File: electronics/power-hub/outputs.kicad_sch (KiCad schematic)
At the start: 72 parts, among them J2 ROW A, J3 ROW B, J4 ROW C, J5 ROW D, U11 TPS26600PWPR, U12 TPS26600PWPR, U13 TPS26600PWPR, U14 TPS26600PWPR

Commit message: PCBA review: hub and node fixes before the order
On main's CH224A hub and the bay node v0.5.

Power hub:
- CPL: the side LEDs (C598310, C4555382) +0.825 mm, their polarity
  proven from JLC's own footprints (and C495809 at 270 deg in the table,
  for the IRF7842 the AP33772S hub had).
- Rows: SHDN pull-downs 10k, so rows stay off without firmware (100k
  gave 1 V at the pin's 10 uA); a B5819W at each row output for the
  cable's kick; the red FAULT LEDs fed from their ROW_EN, so a row that
  is simply off shows no fault.
- In2's VRACK band 8 mm wide; the console's USB pair hand-routed on
  F.Cu over In1 (U5's channels in the pair's order), EN's capacitor at
  the module's pin; reliefs on both pads of C2, C10, R3, C11-C14; notes
  corrected, the outputs sheet on A2.
- The PESD2CAN kept and documented (no stocked CAN TVS stays off at
  29.4 V and clamps under +40 V).

Bay node:
- SW3 placed on its pegs (-0.55 mm, Shouhan's land pattern); 2.2k I2C
  pull-ups; POS_IN 470k; AUX_VREF 1k; 100k on SVC; U9's input on a +5V
  island with three vias, C20 at its pins; C12 relieved; the camera note
  and the catalog's MPN text corrected.

Both re-routed: ERC 0, DRC 0 (the known C8 silkscreen warning), parity
0; CPL audit against JLC's footprints: every part agrees but SW3's pads
(0.13 mm, on purpose).  Bring-up measurements in assembly.md, the
resolution in pcba-review.md.

Co-Authored-By: Claude Opus 5.5 <noreply@anthropic.com>
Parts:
- added D41, D42, D43, D44: B5819W SL, Diode_SMD:D_SOD-123, symbol Device:D_Schottky
- R71, R72, R73, R74: value 100k -> 10k; LCSC C25803 -> C25804; MPN 0603WAF1003T5E -> 0603WAF1002T5E
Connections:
- net +3V3: no longer R51.1, R52.1, R53.1, R54.1
- net GND: now also D41.2 (A), D42.2 (A), D43.2 (A), D44.2 (A)
- net ROW_A: now also D41.1 (K)
- net ROW_B: now also D42.1 (K)
- net ROW_C: now also D43.1 (K)
- net ROW_D: now also D44.1 (K)
- net ROW_EN_A: now also R51.1
- net ROW_EN_B: now also R52.1
- net ROW_EN_C: now also R53.1
- net ROW_EN_D: now also R54.1
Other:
- moved on the sheet: C12, C13, C14, C22, C23, C24, C32, C33, C34, C62, C63, C64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

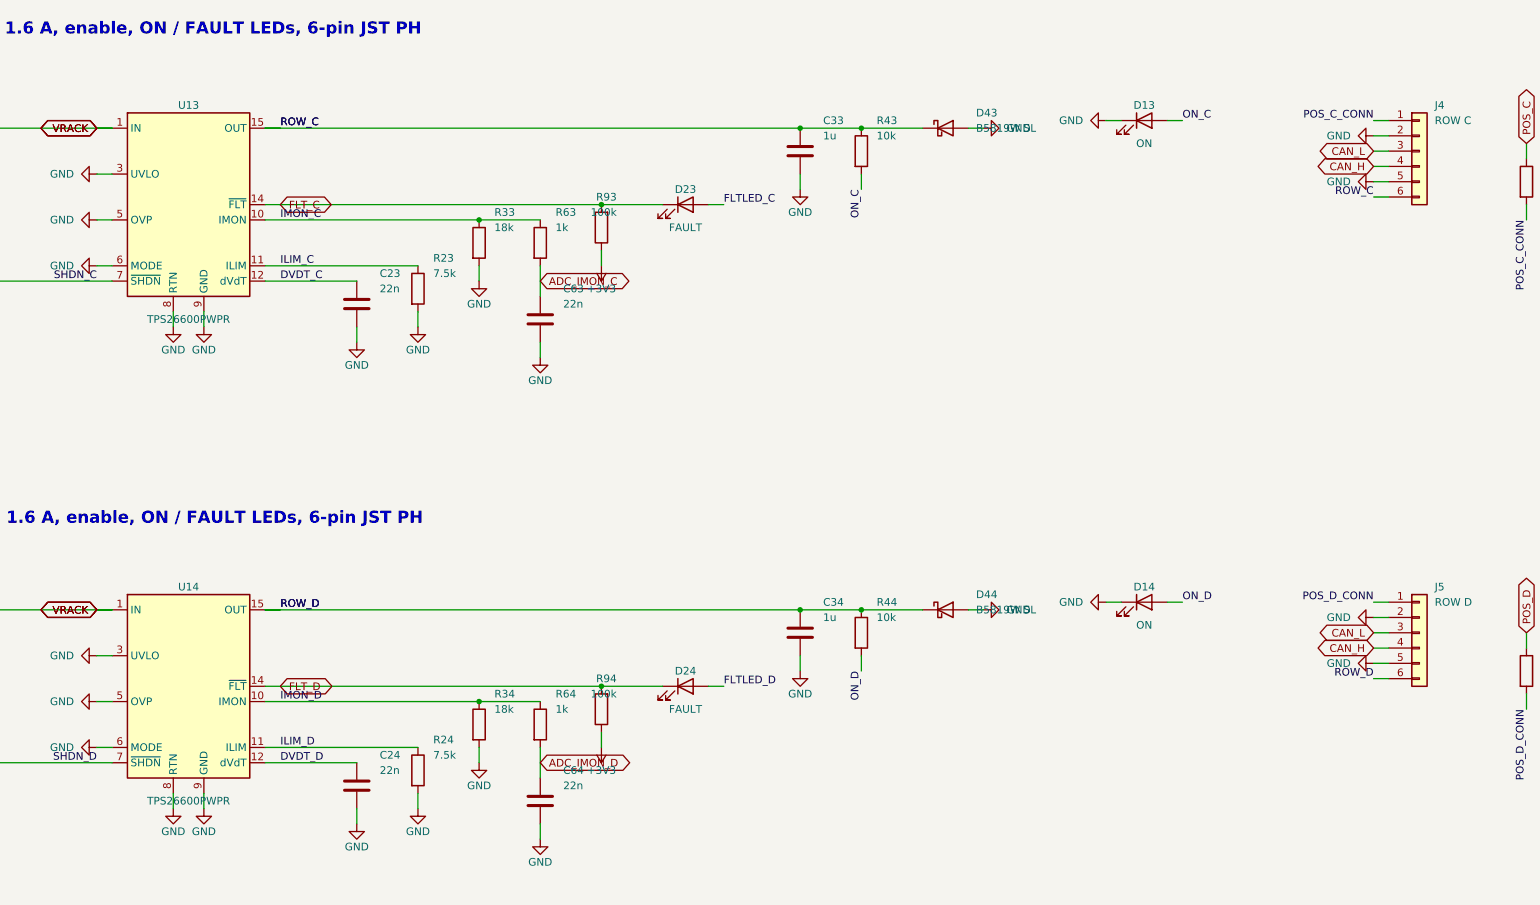
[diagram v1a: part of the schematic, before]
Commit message: Power hub: rows C and D not fitted for now
The user: "ne montons pas C et D pour l'instant".  The rack has two
rows, so the hub's rows C and D keep their footprints and routing, and
their costly parts are DNP:
- the eFuses U13/U14;
- the connectors J4/J5;
- the front LEDs D13/D14 (ON) and D23/D24 (FAULT).

Their passives stay: FLT's pull-up keeps FLT high and the IMON
resistor keeps IMON at 0 V, so the firmware sees no phantom fault or
current.  design.py's FITTED lists the fitted rows.

* The schematic and the PCB carry KiCad's DNP flag on those eight
  parts, set without touching placement or routing.  ERC 0, DRC 0,
  unconnected 0, parity 0.
* Fab outputs: the JLC BOM and CPL leave the eight out.  The Gerbers
  are unchanged (compared, member by member, minus dates).  The
  renders show the bare pads.
* The viewer shows the board as built: the fab GLB is exported with
  --no-dnp (the STEP keeps the DNP parts for fit checks).  The 3D
  coverage report lists them as "dnp", not missing.  The hub's viewer
  model is rebuilt.
* BOM regenerated.  The quote isn't repriced yet: the hub's balancing
  "components" line absorbs the difference until the cost session's
  pass.
* Docs: electronics.md and power.md say what refitting a row takes: a
  hot plate and hot air for the eFuse's pad, the LEDs on the box's
  holes, the devicetree, and the 140 W charger for a third row.

96 tools tests OK.

Co-Authored-By: Claude Opus 5.5 <noreply@anthropic.com>
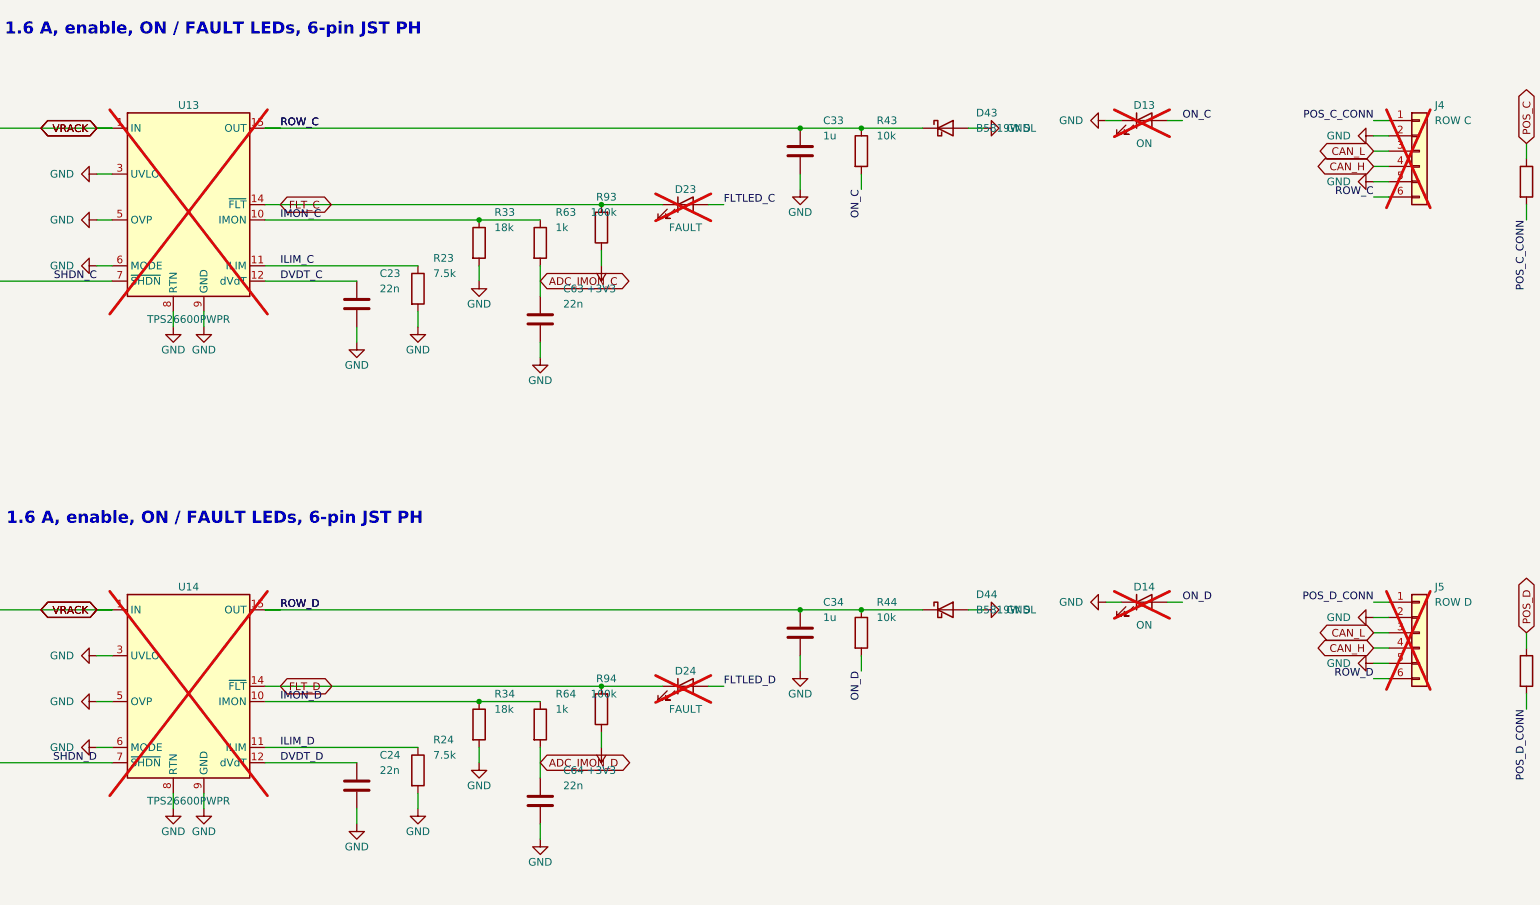
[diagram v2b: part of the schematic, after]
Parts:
- D13, D14, D23, D24, J4, J5, U13, U14: now not fitted
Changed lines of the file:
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@@
 		(in_bom yes)
 		(on_board yes)
-		(dnp no)
+		(dnp yes)
 		(fields_autoplaced yes)
 		(property "Reference" "U13"
@@
 		(in_bom yes)
 		(on_board yes)
-		(dnp no)
+		(dnp yes)
 		(fields_autoplaced yes)
 		(property "Reference" "D23"
@@
 		(in_bom yes)
 		(on_board yes)
-		(dnp no)
+		(dnp yes)
 		(fields_autoplaced yes)
 		(property "Reference" "D13"
@@
 		(in_bom yes)
 		(on_board yes)
-		(dnp no)
+		(dnp yes)
 		(fields_autoplaced yes)
 		(property "Reference" "J4"
@@
 		(in_bom yes)
 		(on_board yes)
-		(dnp no)
+		(dnp yes)
 		(fields_autoplaced yes)
 		(property "Reference" "U14"
@@
 		(in_bom yes)
 		(on_board yes)
-		(dnp no)
+		(dnp yes)
 		(fields_autoplaced yes)
 		(property "Reference" "D24"
@@
 		(in_bom yes)
 		(on_board yes)
-		(dnp no)
+		(dnp yes)
 		(fields_autoplaced yes)
 		(property "Reference" "D14"
@@
 		(in_bom yes)
 		(on_board yes)
-		(dnp no)
+		(dnp yes)
 		(fields_autoplaced yes)
 		(property "Reference" "J5"

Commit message: Power hub: 47 nF soft start, the LMR51625, the controller sheet on A2
Fixes from the schematic counter-review that the user approved.

* Every 22 nF goes to 47 nF.  The new part is C1622 (basic, the same
  0603 pads).  It covers C21-C24 (eFuse dVdT), C61-C64 (the IMON
  filter, now 47 us) and C118/C119 (the CAN split terminations).
  - A row of four nodes is about 450 uF.  With 22 nF the soft start
    charged it at about 2.6 A, over the 1.6 A limit.
  - With 47 nF it charges at about 1.2 A.  The ramp is 7.5 ms at 20 V
    and 10.5 ms at 28 V (t = 8e3 x V_IN x C_dVdT).
  - passives.py and its cache gain the 47 nF.
* The hub firmware's FLT blanking goes from 10 ms to 25 ms
  (HUB_ROW_FLT_BLANK_MS).  The TPS2660 asserts FLT through its soft
  start, and at 28 V that start now lasts 10.5 ms, longer than 10 ms.
* The buck changes from the LMR51635 to the LMR51625 with the 4.7 uH
  FXL0630-4R7-M.  These are the node's pair (buck25 / buck_l47, TI
  SLUSF64B table 8-1).
  - The controller takes under 0.7 A.
  - Same pinout and footprint, so the same 270 deg CPL correction.
* The routed PCB keeps its routing.  Only the properties of those 12
  footprints change (value, MPN, LCSC, description, datasheet).  They
  were copied from design.py with KiCad's Python, as pcbgen places
  them.
* The controller sheet (page 4) goes on A2, so the CAN block, the
  mounting holes and the notes are now on the page.
* Stale notes corrected:
  - the charger: 100 W at 20 V by default, 140 W EPR as an option;
  - the TPS26600's internal OVP is 31-34 V (typ 32.6 V), not 33 V
    (design.py, power.md, the devicetree comment);
  - the buck block now reads "from VRACK": there is no input switch
    any more.

Regenerated on zephyrbox with kicad.sh power-hub --check --fab.
- ERC 0, DRC 0, unconnected 0, parity 0.
- The Gerber zip and the top and iso renders are the same content.
  The bottom render's only difference was 9 pixels of raytracer
  noise in via holes, so it is kept.
- The viewer GLB com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
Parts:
- C21, C22, C23, C24, C61, C62, C63, C64: value 22n -> 47n; LCSC C21122 -> C1622; MPN CL10B223KB8NNNC -> CL10B473KB8NNNC
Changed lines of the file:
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@@
 			)
 		)
-		(property "Value" "22n"
+		(property "Value" "47n"
 			(at 120.65 71.12 0)
 			(effects
@@
 			)
 		)
-		(property "Description" "Capacitor 22n 0603"
+		(property "Description" "Capacitor 47n 0603"
 			(at 116.84 73.66 0)
 			(effects
@@
 			)
 		)
-		(property "LCSC" "C21122"
+		(property "LCSC" "C1622"
 			(at 116.84 73.66 0)
 			(effects
@@
 			)
 		)
-		(property "MPN" "CL10B223KB8NNNC"
+		(property "MPN" "CL10B473KB8NNNC"
 			(at 116.84 73.66 0)
 			(effects
@@
 			)
 		)
-		(property "Value" "22n"
+		(property "Value" "47n"
 			(at 151.13 73.66 0)
 			(effects
@@
 			)
 		)
-		(property "Description" "Capacitor 22n 0603"
+		(property "Description" "Capacitor 47n 0603"
 			(at 147.32 76.2 0)
 			(effects
@@
 			)
 		)
-		(property "LCSC" "C21122"
+		(property "LCSC" "C1622"
 			(at 147.32 76.2 0)
 			(effects
@@
 			)
 		)
-		(property "MPN" "CL10B223KB8NNNC"
+		(property "MPN" "CL10B473KB8NNNC"
 			(at 147.32 76.2 0)
 			(effects
@@
 			)
 		)
-		(property "Value" "22n"
+		(property "Value" "47n"
 			(at 120.65 151.13 0)
 			(effects
@@
 			)
 		)
-		(property "Description" "Capacitor 22n 0603"
+		(property "Description" "Capacitor 47n 0603"
 			(at 116.84 153.67 0)
 			(effects
@@
 			)
 		)
-		(property "LCSC" "C21122"
+		(property "LCSC" "C1622"
 			(at 116.84 153.67 0)
 			(effects
@@
 			)
 		)
-		(property "MPN" "CL10B223KB8NNNC"
+		(property "MPN" "CL10B473KB8NNNC"
 			(at 116.84 153.67 0)
 			(effects
@@
 			)
 		)
-		(property "Value" "22n"
+		(property "Value" "47n"
 			(at 151.13 153.67 0)
 			(effects
@@
 			)
 		)
-		(property "Description" "Capacitor 22n 0603"
+		(property "Description" "Capacitor 47n 0603"
 			(at 147.32 156.21 0)
 			(effects
@@
 			)
 		)
-		(property "LCSC" "C21122"
+		(property "LCSC" "C1622"
 			(at 147.32 156.21 0)
 			(effects
@@
 			)
 		)
-		(property "MPN" "CL10B223KB8NNNC"
+		(property "MPN" "CL10B473KB8NNNC"
 			(at 147.32 156.21 0)
 			(effects
@@
 			)
 		)
-		(property "Value" "22n"
+		(property "Value" "47n"
 			(at 120.65 232.41 0)
 			(effects
@@
 			)
 		)
-		(property "Description" "Capacitor 22n 0603"
+		(property "Description" "Capacitor 47n 0603"
 			(at 116.84 234.95 0)
 			(effects
@@
 			)
 		)
-		(property "LCSC" "C21122"
+		(property "LCSC" "C1622"
 			(at 116.84 234.95 0)
 			(effects
@@
 			)
 		)
-		(property "MPN" "CL10B223KB8NNNC"
+		(property "MPN" "CL10B473KB8NNNC"
 			(at 116.84 234.95 0)
 			(effects
@@
 			)
 		)
-		(property "Value" "22n"
+		(property "Value" "47n"
 			(at 151.13 234.95 0)
 			(effects
@@
 			)
 		)
-		(property "Description" "Capacitor 22n 0603"
+		(property "Description" "Capacitor 47n 0603"
 			(at 147.32 237.49 0)
 			(effects
@@
 			)
 		)
-		(property "LCSC" "C21122"
+		(property "LCSC" "C1622"
 			(at 147.32 237.49 0)
 			(effects
@@
 			)
 		)
-		(property "MPN" "CL10B223KB8NNNC"
+		(property "MPN" "CL10B473KB8NNNC"
 			(at 147.32 237.49 0)
 			(effects
@@
 			)
 		)
-		(property "Value" "22n"
+		(property "Value" "47n"
 			(at 120.65 312.42 0)
 			(effects
@@
 			)
 		)
-		(property "Description" "Capacitor 22n 0603"
+		(property "Description" "Capacitor 47n 0603"
 			(at 116.84 314.96 0)
 			(effects
@@
 			)
 		)
-		(property "LCSC" "C21122"
+		(property "LCSC" "C1622"
 			(at 116.84 314.96 0)
 			(effects
@@
 			)
 		)
-		(property "MPN" "CL10B223KB8NNNC"
+		(property "MPN" "CL10B473KB8NNNC"
 			(at 116.84 314.96 0)
 			(effects
@@
 			)
 		)
-		(property "Value" "22n"
+		(property "Value" "47n"
 			(at 151.13 314.96 0)
 			(effects
@@
 			)
 		)
-		(property "Description" "Capacitor 22n 0603"
+		(property "Description" "Capacitor 47n 0603"
 			(at 147.32 317.5 0)
 			(effects
@@
 			)
 		)
-		(property "LCSC" "C21122"
+		(property "LCSC" "C1622"
 			(at 147.32 317.5 0)
 			(effects
@@
 			)
 		)
-		(property "MPN" "CL10B223KB8NNNC"
+		(property "MPN" "CL10B473KB8NNNC"
 			(at 147.32 317.5 0)
 			(effects
@@
 		)
 	)
-	(text_box "TPS26600: I_LIM ≈ 12 A·kΩ / R_ILIM → 7.5k ≈ 1.6 A (JST PH: 2 A per contact).\nt_dVdT = 8e3 · V_IN · C_dVdT → 22 nF ≈ 3.5 ms at 20 V, 4.9 ms at 28 V.\nIMON: 78 µA/A into 18k → 1.4 V/A (2.2 V at the limit), 1k + 22 nF to the ESP32's ADC.\nSHDN: 10k to GND (row off: ≤ 10 µA from the pin, 0.1 V), ROW_EN through 10k → 1.65 V (on above 0.94 V).\nThe firmware holds ROW_EN with the ESP32's GPIO hold, so a controller reset leaves the rows as they were.\nFLT: open drain, 100k to 3.3 V for the controller; the red LED (1k) is fed from ROW_EN: it lights only for\n  a fault on an enabled row (FLT is also low while a row is off or starting).\nD41–D44 B5819W: GND → each row's output at its connector, for the cable's kick when the eFuse cuts a short.\nUVLO / OVP / MODE to GND: internal 15 V / 33 V thresholds, current-limit mode, auto-retry."
+	(text_box "TPS26600: I_LIM ≈ 12 A·kΩ / R_ILIM → 7.5k ≈ 1.6 A (JST PH: 2 A per contact).\nt_dVdT = 8e3 · V_IN · C_dVdT → 47 nF ≈ 7.5 ms at 20 V, 10.5 ms at 28 V.  A row of four nodes (≈ 450 µF)\n  then charges at C / (8e3 · C_dVdT) ≈ 1.2 A, under the 1.6 A limit (22 nF needed ≈ 2.6 A).\nIMON: 78 µA/A into 18k → 1.4 V/A (2.2 V at the limit), 1k + 47 nF (47 µs) to the ESP32's ADC.\nSHDN: 10k to GND (row off: ≤ 10 µA from the pin, 0.1 V), ROW_EN through 10k → 1.65 V (on above 0.94 V).\nThe firmware holds ROW_EN with the ESP32's GPIO hold, so a controller reset leaves the rows as they were.\nFLT: open drain, 100k to 3.3 V for the controller; the red LED (1k) is fed from ROW_EN: it lights only for\n  a fault on an enabled row (FLT is also low while a row is off or starting).\nD41–D44 B5819W: GND → each row's output at its connector, for the cable's kick when the eFuse cuts a short.\nUVLO / OVP / MODE to GND: internal 15 V / 31–34 V (typ 32.6 V) thresholds, current-limit mode, auto-retry."
 		(exclude_from_sim no)
 		(at 20.32 353.06 0)
-		(size 414.02 25.4)
+		(size 414.02 26.67)
 		(margins 1.5 1.5 1.5 1.5)
 		(stroke

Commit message: Schematic review S1, S4, S6: POS_IN 150k, the hub's ON LEDs on 18k, the camera's 0.75 A PTC
The user approved them ("S1 oui / S6 oui / S4 oui").

* S1, bay node: R29 470k -> 150k (C22807, basic).
  - Before its firmware runs, the upstream POS output (a node's IO42, the
    hub's IO10-13) floats. The BAT54S's warm leakage (about 2-3 uA at
    65 C) could then lift POS_IN through 470k to VIL.
  - Driven high through R30 + R28, 150k still gives 2.87 V, above VIH.
  - The design.py notes and bay_node.dtsi follow.
* S4, power hub: R41-R44 (the ON LEDs on the row outputs) 10k -> 18k
  (C25810, already on the board): 1.4 mA and 37 mW at 28 V. The 10k
  ran at 75 % of its 0603 rating at 29.4 V.
* S6, bay node: F1 (CAM_5V) goes from the 0.5 A PTC to SMD1206P075TF
  (RUILON, C20987, new catalog key pptc750): 0.75 A hold, 1.5 A trip,
  the same 1206 footprint. It is extended like C20799, so no fee changes.
  - Arducam gives the Mega 317 mA working: with the LEDs that is
    ~0.42 A on CAM_5V, where the 0.5 A part holds ~0.31 A at 70 C.
  - The camera pod's LDO tab gets the copper its routing leaves: a
    top-side +3V3 pour round the tab and a bottom-side island, joined by
    three vias. U1 drops ~0.5 W at 317 mA. The routing is unchanged.
  - The "~120 mA" notes go to 317 mA (node and pod design.py,
    electronics.md).
  - The bay's worst case follows: <= 2.25 A on +5V, the buck's inductor
    peaking at ~2.65 A (under its 2.9 A minimum limit), 13.5 W from
    VRACK (power-distribution-review.md, the buck notes).

The routed PCBs keep their routing.
- Node and hub: only the changed parts' properties (KiCad's Python, as
  pcbgen sets them).
- Pod: the two new zones and three vias, refilled.
- ERC 0, DRC 0, unconnected 0, parity 0 on all three (run on the Mac:
  zephyrbox didn't answer).
- keep_unchanged kept the node's renders and the hub's Gerbers. The
  hub's bottom render is restored: 9 pixels of via-hole noise, as before.
- The pod's renders, Gerbers and viewer GLB chang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
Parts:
- R41, R42, R43, R44: value 10k -> 18k; LCSC C25804 -> C25810; MPN 0603WAF1002T5E -> 0603WAF1802T5E
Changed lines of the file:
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@@
 			)
 		)
-		(property "Value" "10k"
+		(property "Value" "18k"
 			(at 203.2 45.72 0)
 			(effects
@@
 			)
 		)
-		(property "Description" "Resistor 10k 0603"
+		(property "Description" "Resistor 18k 0603"
 			(at 200.66 48.26 0)
 			(effects
@@
 			)
 		)
-		(property "LCSC" "C25804"
+		(property "LCSC" "C25810"
 			(at 200.66 48.26 0)
 			(effects
@@
 			)
 		)
-		(property "MPN" "0603WAF1002T5E"
+		(property "MPN" "0603WAF1802T5E"
 			(at 200.66 48.26 0)
 			(effects
@@
 			)
 		)
-		(property "Value" "10k"
+		(property "Value" "18k"
 			(at 203.2 125.73 0)
 			(effects
@@
 			)
 		)
-		(property "Description" "Resistor 10k 0603"
+		(property "Description" "Resistor 18k 0603"
 			(at 200.66 128.27 0)
 			(effects
@@
 			)
 		)
-		(property "LCSC" "C25804"
+		(property "LCSC" "C25810"
 			(at 200.66 128.27 0)
 			(effects
@@
 			)
 		)
-		(property "MPN" "0603WAF1002T5E"
+		(property "MPN" "0603WAF1802T5E"
 			(at 200.66 128.27 0)
 			(effects
@@
 			)
 		)
-		(property "Value" "10k"
+		(property "Value" "18k"
 			(at 203.2 207.01 0)
 			(effects
@@
 			)
 		)
-		(property "Description" "Resistor 10k 0603"
+		(property "Description" "Resistor 18k 0603"
 			(at 200.66 209.55 0)
 			(effects
@@
 			)
 		)
-		(property "LCSC" "C25804"
+		(property "LCSC" "C25810"
 			(at 200.66 209.55 0)
 			(effects
@@
 			)
 		)
-		(property "MPN" "0603WAF1002T5E"
+		(property "MPN" "0603WAF1802T5E"
 			(at 200.66 209.55 0)
 			(effects
@@
 			)
 		)
-		(property "Value" "10k"
+		(property "Value" "18k"
 			(at 203.2 287.02 0)
 			(effects
@@
 			)
 		)
-		(property "Description" "Resistor 10k 0603"
+		(property "Description" "Resistor 18k 0603"
 			(at 200.66 289.56 0)
 			(effects
@@
 			)
 		)
-		(property "LCSC" "C25804"
+		(property "LCSC" "C25810"
 			(at 200.66 289.56 0)
 			(effects
@@
 			)
 		)
-		(property "MPN" "0603WAF1002T5E"
+		(property "MPN" "0603WAF1802T5E"
 			(at 200.66 289.56 0)
 			(effects
